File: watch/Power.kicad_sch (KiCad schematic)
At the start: 17 parts, among them IC401 nPM1300-QEXX, X402 Battery

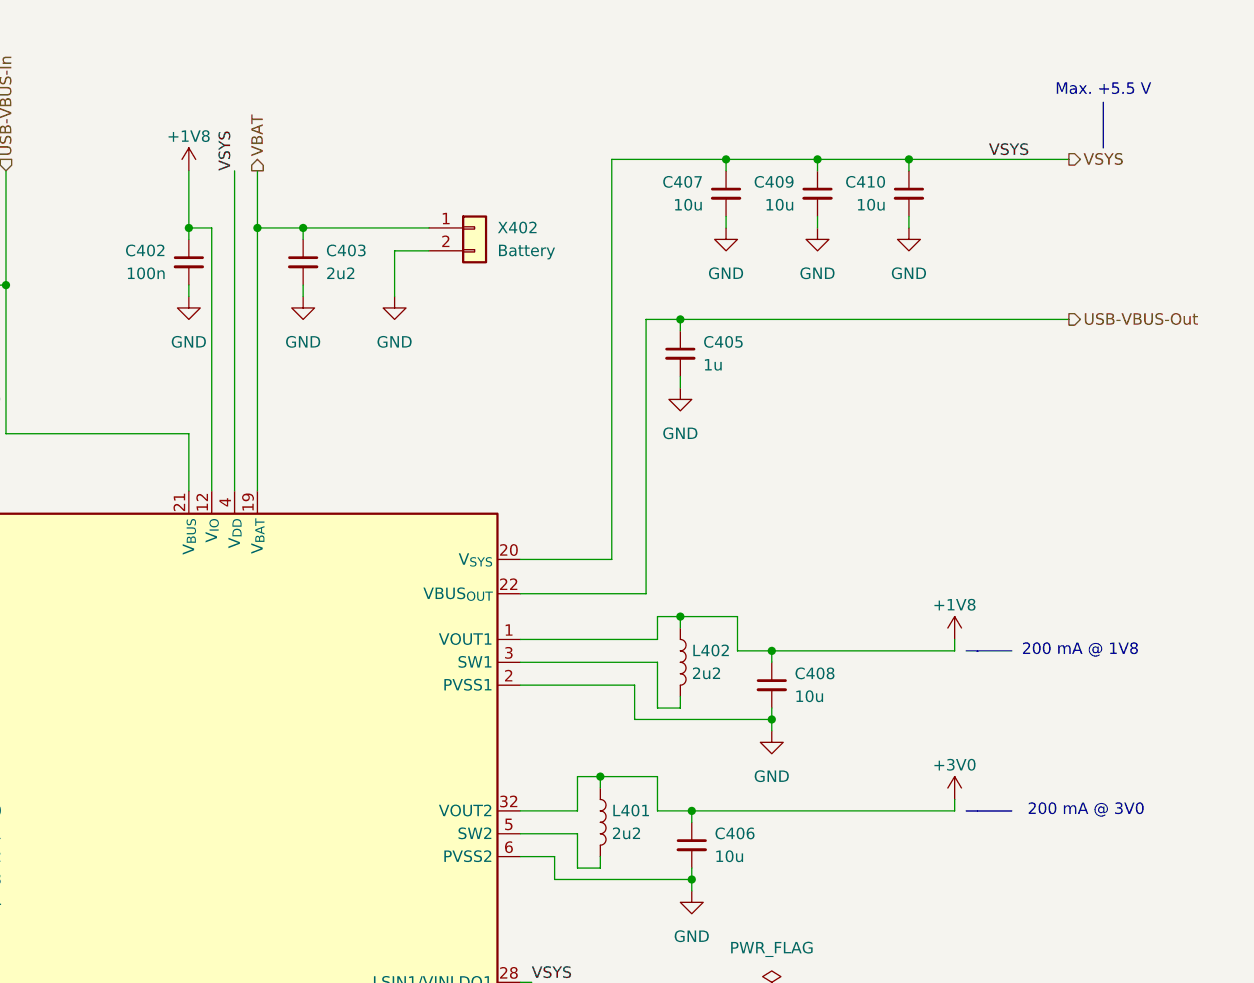
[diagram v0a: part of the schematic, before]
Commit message: Bug: Issue #14
- Change 3V0 to 3V3 to prevent flickering display

Closes: #14

Signed-off-by: Daniel Kampert <DanielKampert@kampis-elektroecke.de>
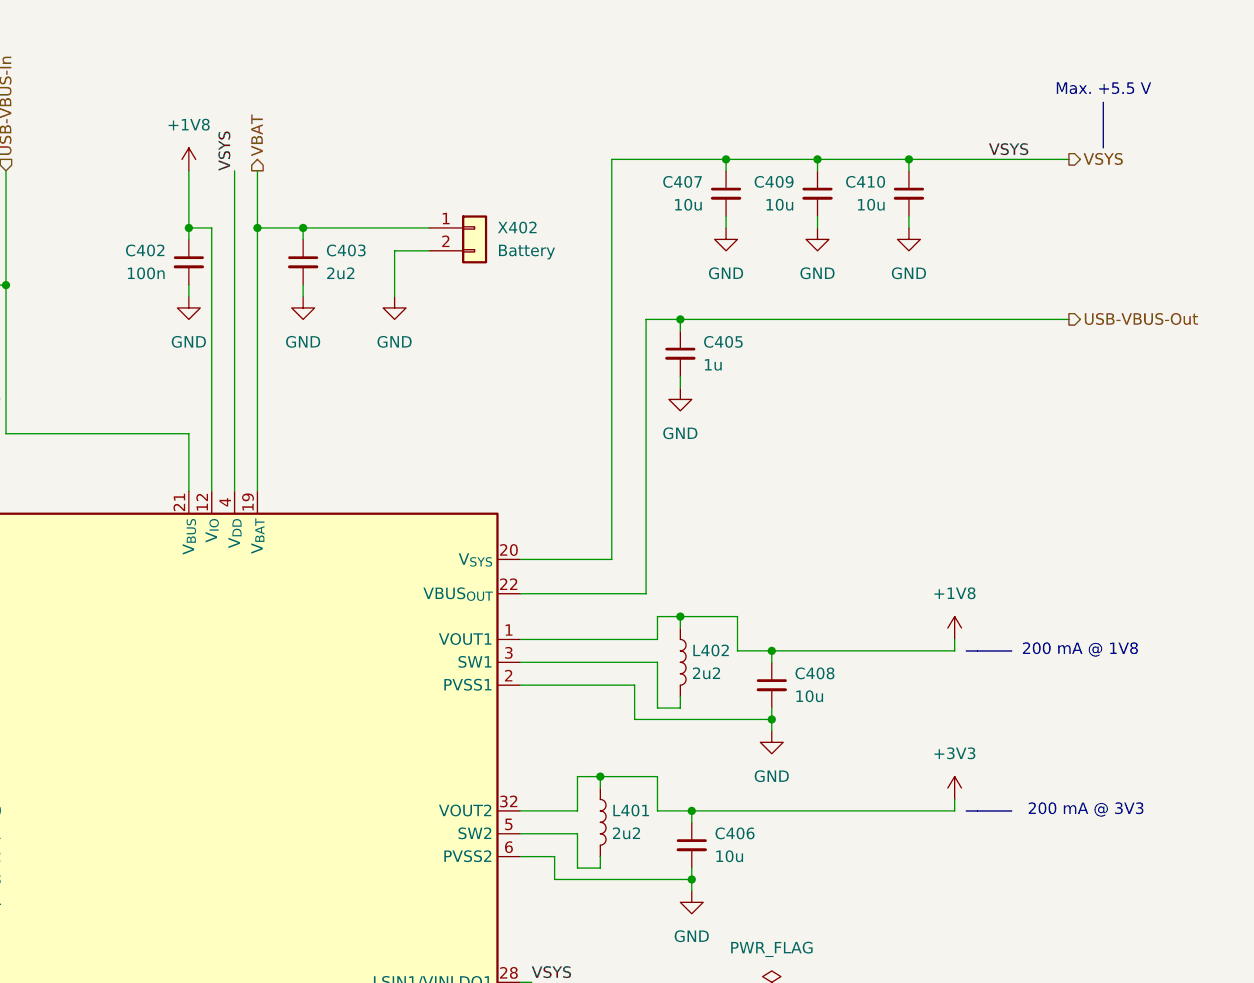
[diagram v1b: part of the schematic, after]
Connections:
- net +3V0 renamed +3V3
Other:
- note added: "200 mA @ 3V3"
- note removed: "200 mA @ 3V0"
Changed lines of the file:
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@@
 		)
 	)
-	(text "200 mA @ 3V0"
+	(text "200 mA @ 3V3"
 		(exclude_from_sim no)
 		(at 266.065 101.6 0)
@@
 		(dnp no)
 		(fields_autoplaced yes)
-		(property "Reference" "#PWR0411"
+		(property "Reference" "#PWR411"
 			(at 166.37 34.29 0)
 			(effects
@@
 		)
 		(property "Value" "+1V8"
-			(at 166.37 26.67 0)
+			(at 166.37 25.4 0)
 			(effects
 				(font
@@
 			(project "ZSWatch"
 				(path "/d5742f03-3b1a-42e5-a384-018bd4b919aa/c5103ceb-5325-4a84-a025-9638a412984e/cee9a3a2-28cd-4e6c-b23d-337f115f39e8"
-					(reference "#PWR0411")
+					(reference "#PWR411")
 					(unit 1)
 				)
@@
 	)
 	(symbol
-		(lib_id "power:+3V0")
+		(lib_id "power:+3V3")
 		(at 251.46 100.33 0)
 		(unit 1)
@@
 		(dnp no)
 		(fields_autoplaced yes)
-		(property "Reference" "#PWR0427"
+		(property "Reference" "#PWR427"
 			(at 251.46 104.14 0)
 			(effects
@@
 			)
 		)
-		(property "Value" "+3V0"
-			(at 251.46 96.52 0)
+		(property "Value" "+3V3"
+			(at 251.46 95.25 0)
 			(effects
 				(font
@@
 			)
 		)
-		(property "Description" "Power symbol creates a global label with name \"+3V0\""
+		(property "Description" "Power symbol creates a global label with name \"+3V3\""
+			(at 251.46 100.33 0)
+			(effects
+				(font
+					(size 1.27 1.27)
+				)
+				(hide yes)
+			)
+		)
+		(property "manf" ""
+			(at 251.46 100.33 0)
+			(effects
+				(font
+					(size 1.27 1.27)
+				)
+				(hide yes)
+			)
+		)
+		(property "manf#" ""
+			(at 251.46 100.33 0)
+			(effects
+				(font
+					(size 1.27 1.27)
+				)
+				(hide yes)
+			)
+		)
+		(property "mouser#" ""
 			(at 251.46 100.33 0)
 			(effects
@@
 			(project "Dev-Kit"
 				(path "/d5742f03-3b1a-42e5-a384-018bd4b919aa/c5103ceb-5325-4a84-a025-9638a412984e/cee9a3a2-28cd-4e6c-b23d-337f115f39e8"
-					(reference "#PWR0427")
+					(reference "#PWR427")
 					(unit 1)
 				)
@@
 		(dnp no)
 		(fields_autoplaced yes)
-		(property "Reference" "#PWR0426"
+		(property "Reference" "#PWR426"
 			(at 251.46 86.36 0)
 			(effects
@@
 		)
 		(property "Value" "+1V8"
-			(at 251.46 78.74 0)
+			(at 251.46 77.47 0)
 			(effects
 				(font
@@
 			)
 		)
+		(property "manf" ""
+			(at 251.46 82.55 0)
+			(effects
+				(font
+					(size 1.27 1.27)
+				)
+				(hide yes)
+			)
+		)
+		(property "manf#" ""
+			(at 251.46 82.55 0)
+			(effects
+				(font
+					(size 1.27 1.27)
+				)
+				(hide yes)
+			)
+		)
+		(property "mouser#" ""
+			(at 251.46 82.55 0)
+			(effects
+				(font
+					(size 1.27 1.27)
+				)
+				(hide yes)
+			)
+		)
 		(pin "1"
 		)
@@
 			(project "ZSWatch"
 				(path "/d5742f03-3b1a-42e5-a384-018bd4b919aa/c5103ceb-5325-4a84-a025-9638a412984e/cee9a3a2-28cd-4e6c-b23d-337f115f39e8"
-					(reference "#PWR0426")
+					(reference "#PWR426")
 					(unit 1)
 				)
